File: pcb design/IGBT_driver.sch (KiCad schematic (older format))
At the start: 52 parts, among them J2 DESAT, Q13 NPN, Q14 PNP, U1 ISO5852S, U13 LM3480, U6 NAND, U8 TLP2745

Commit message: Changed power supply from 15/-8V to +15/-15V se we can make better use uf programmable -VEE. Changed connector to 14pos. Connected some missing signals. Updated layout
Signed-off-by: Marcos Chaparro <mchaparro@paltatech.com>
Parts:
- removed C53: 100nF, IPC7351-Nominal:CAPC1608X55, symbol C-0603
- removed D15: BAT54S, smd-semi:SOT-23, symbol BAT54S
- removed U6: NAND, smd-semi:SOT-23-5, symbol 741G00-SOT23
- added D15: 1N4148W, smd-semi:SOD-123, symbol 1N4148W
- added D17: GSOT03C, smd-semi:SOT-23, symbol BAT54A
- added R93: 330R, IPC7351-Nominal:RESC1608X50, symbol R-0603
- U8: value TLP2745 -> SI8710B; #mfg TLP2745(TP,E -> (none); mfg# (none) -> SI8710BD-B-IS; replacement SI8710BD-B-IS -> TLP2745(TP,E
- U8: value TLP2745 -> SI8710B; #mfg TLP2745(TP,E -> (none); mfg# (none) -> SI8710BD-B-IS
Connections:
- net labels added: -15V, IN-, PWM_VEE
- net labels removed: -8V
- wire segments 134 -> 135
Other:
- note added: "When FAULT is asserted\nexternally, mute the input"
- note added: "input protection.\nYou don't want a latch-up here"
- note removed: "Global Shutdown and reset configuration.\nEnsures that when ANY driver faults, all of\nthem are turned off. Datasheet: 10.2.2.5"
- note removed: "Input protection"
- note removed: "Inverts the signal so we\ncan use a positive logic\nAND fault mute-ing"
- moved on the sheet: C48, R42, R43, R45, TP13, TP14

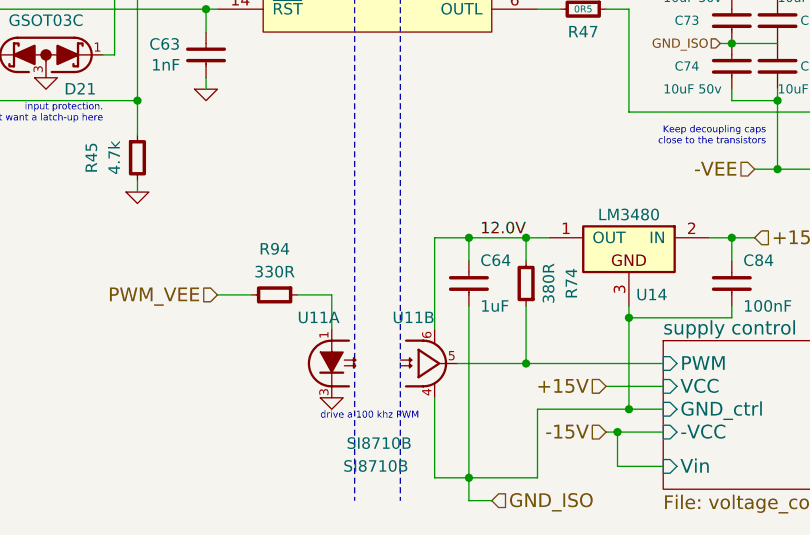
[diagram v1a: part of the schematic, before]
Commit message: Changed isolated amplifier from AMC1200 to AMC1301 because it has reinforced isolation. This required a different layout
Signed-off-by: Marcos Chaparro <mchaparro@paltatech.com>
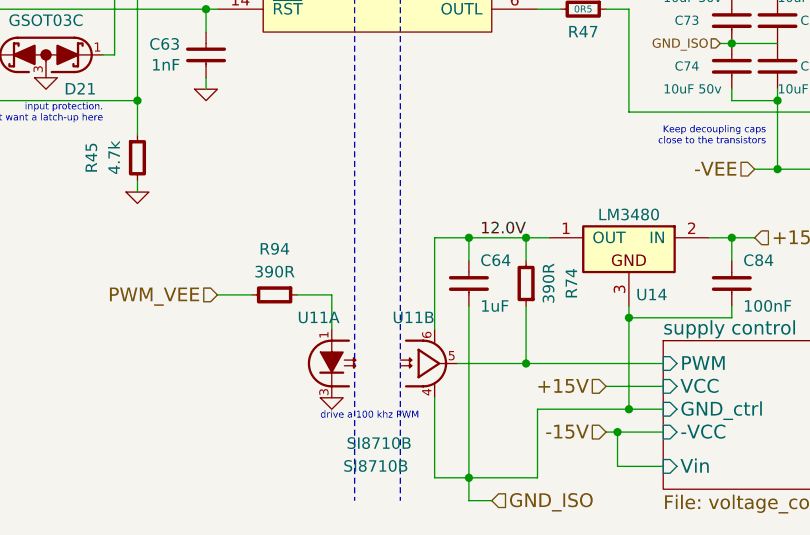
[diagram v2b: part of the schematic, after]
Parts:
- C16: mfg# (none) -> C0805C101J5GACTU
- D3, D4: #mfg MURS160-13-F -> (none); mfg# (none) -> MURS160-13-F
- R68: value 380R -> 390R; BOM RES SMD 1k 5% [0603] -> RES SMD 390R 1% [0603]; mfg# (none) -> RC0603FR-07390RL
- R93: value 330R -> 390R; BOM RES SMD 1k 5% [0603] -> RES SMD 390R 1% [0603]; mfg# (none) -> RC0603FR-07390RL
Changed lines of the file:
@@
 F 2 "Diodes_SMD:Diode-SMB_Standard" H 9500 4400 60  0001 C CNN
 F 3 "" H 9500 4400 60  0000 C CNN
-F 4 "MURS160-13-F" H 9500 4400 60  0001 C CNN "#mfg"
+F 4 "MURS160-13-F" H 9500 4400 60  0001 C CNN "mfg#"
 	1    9500 4400
 	0    -1   -1   0
@@
 F 2 "Diodes_SMD:Diode-SMB_Standard" H 10100 4400 60  0001 C CNN
 F 3 "" H 10100 4400 60  0000 C CNN
-F 4 "MURS160-13-F" H 10100 4400 60  0001 C CNN "#mfg"
+F 4 "MURS160-13-F" H 10100 4400 60  0001 C CNN "mfg#"
 	1    10100 4400
 	0    -1   -1   0
@@
 F 2 "IPC7351-Nominal:CAPC2012X70" H 8800 4600 50  0001 C CNN
 F 3 "" H 8790 4575 60  0000 C CNN
-F 4 "CAP MLCC 100pF C0G 50V 5% [0805]" H 9600 5150 60  0001 C CNN "BOM"
+F 4 "C0805C101J5GACTU" H 8800 4600 60  0001 C CNN "mfg#"
+F 5 "CAP MLCC 100pF C0G 50V 5% [0805]" H 9600 5150 60  0001 C CNN "BOM"
 	1    8800 4600
 	1    0    0    -1
@@
 AR Path="/58232371/58559E07" Ref="R?"  Part="1"
 F 0 "R74" V 4700 6100 50  0000 C CNN
-F 1 "380R" V 4800 6100 50  0000 C CNN
+F 1 "390R" V 4800 6100 50  0000 C CNN
 F 2 "IPC7351-Nominal:RESC1608X50" H 4900 6100 50  0001 C CNN
 F 3 "" H 4900 6150 60  0000 C CNN
-F 4 "RES SMD 1k 5% [0603]" H 5650 6650 60  0001 C CNN "BOM"
+F 4 "RC0603FR-07390RL" H 4900 6100 60  0001 C CNN "mfg#"
+F 5 "RES SMD 390R 1% [0603]" H 5650 6650 60  0001 C CNN "BOM"
 	1    4900 6100
 	-1   0    0    1
@@
 AR Path="/5824556D/58643F0A" Ref="R94"  Part="1"
 F 0 "R94" V 3600 6150 50  0000 C CNN
-F 1 "330R" V 3700 6150 50  0000 C CNN
+F 1 "390R" V 3700 6150 50  0000 C CNN
 F 2 "IPC7351-Nominal:RESC1608X50" H 3800 6150 50  0001 C CNN
 F 3 "" H 3800 6200 60  0000 C CNN
-F 4 "RES SMD 1k 5% [0603]" H 4550 6700 60  0001 C CNN "BOM"
+F 4 "RC0603FR-07390RL" H 3800 6150 60  0001 C CNN "mfg#"
+F 5 "RES SMD 390R 1% [0603]" H 4550 6700 60  0001 C CNN "BOM"
 	1    3800 6150
 	0    1    1    0

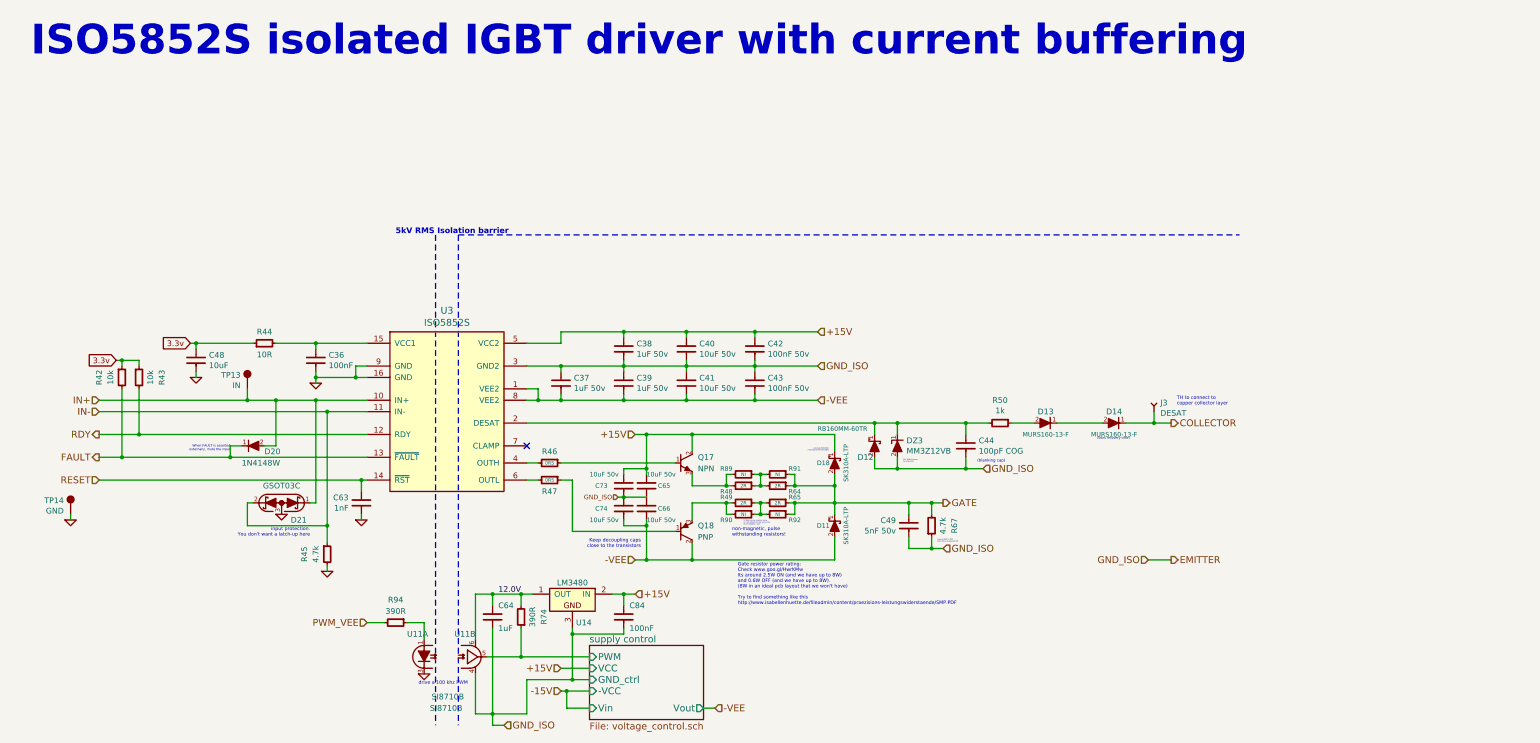
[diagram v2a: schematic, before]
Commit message: For some reasong eyrie needs the schematics and cache file synced
Signed-off-by: Marcos Chaparro <mchaparro@paltatech.com>
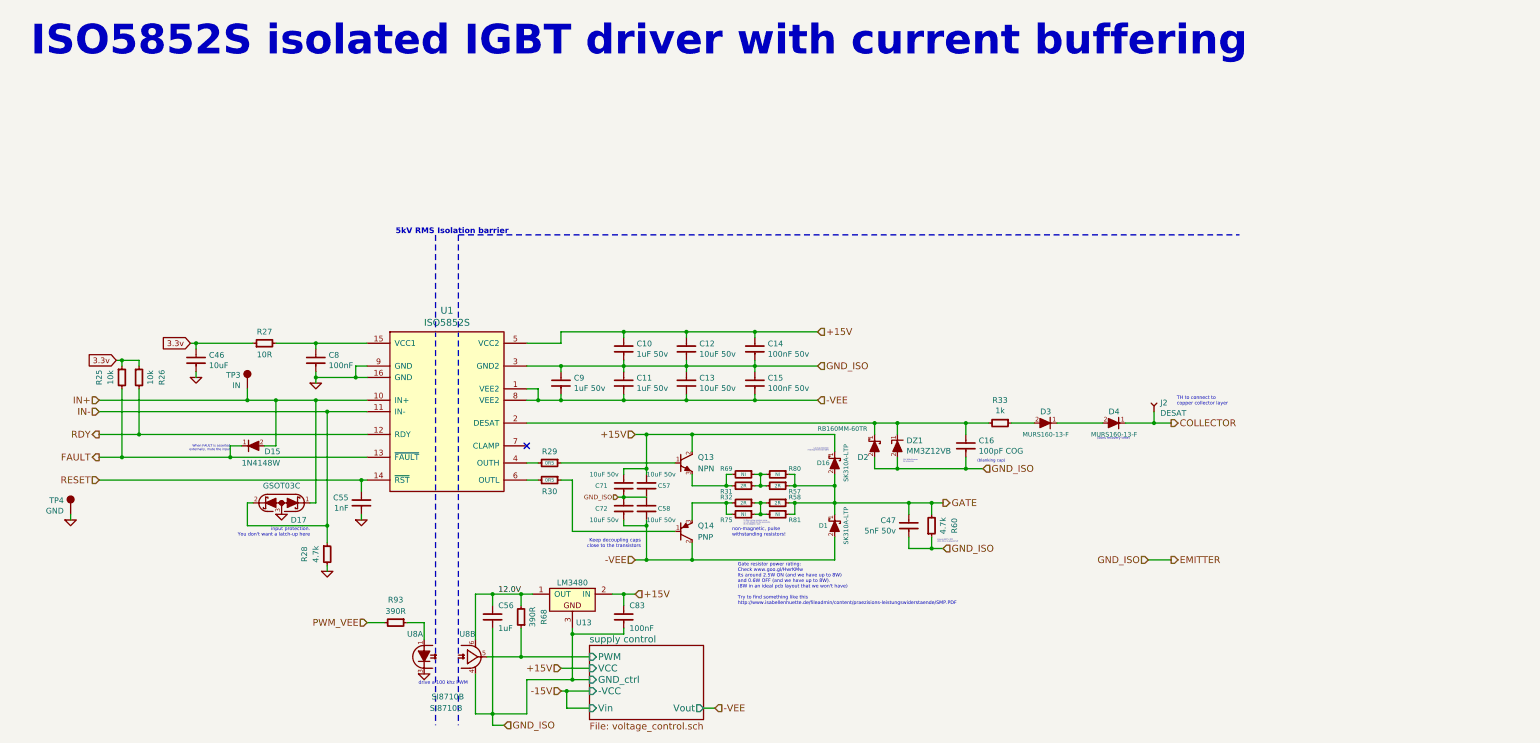
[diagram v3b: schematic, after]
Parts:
- U13: BOM IC MICROCHIP MCP1700T-vv02E/TT -> (none)

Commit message: Larger 2512 gate resistors
Signed-off-by: Marcos Chaparro <mchaparro@paltatech.com>
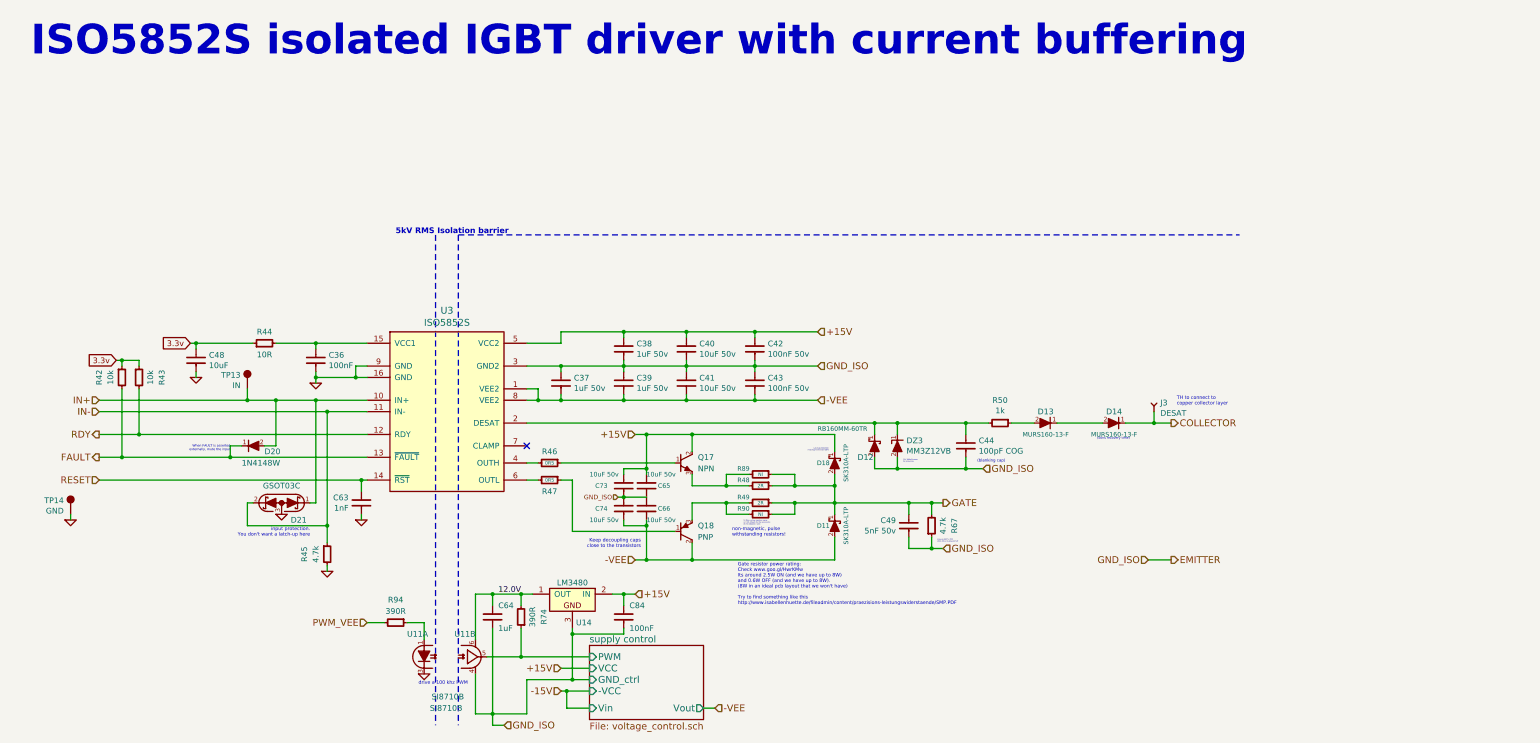
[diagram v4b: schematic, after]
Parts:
- removed R57, R58: 2R, IPC7351-Nominal:RESC3216X60, symbol R-0805
- removed R80, R81: NI, IPC7351-Nominal:RESC3216X60, symbol R-0805
- R31: footprint IPC7351-Nominal:RESC3216X60 -> IPC7351-Nominal:RESC6432X70
- R32, R75: footprint IPC7351-Nominal:RESC3216X60 -> IPC7351-Nominal:RESC6432X70; BOM RES SMD 2R 1% 2W +-100ppm [1206] -> RES SMD 2R 1% 2W +-100ppm [2512]
- R69: footprint IPC7351-Nominal:RESC3216X60 -> IPC7351-Nominal:RESC6432X70; #mfg PCNM1206K2R00FST5 -> (none); BOM RES SMD 2R 1% 2W +-100ppm [1206] -> (none)
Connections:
- net GATE: now also R31.1, R32.1, R69.1, R75.1
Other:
- moved on the sheet: R48, R49, R89, R90

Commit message: Added CERN Open Hardware Licence ("CERN OHL") version 1.2 documents
Signed-off-by: Marcos Chaparro <mchaparro@paltatech.com>
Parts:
- R31: value 2R -> 3R; #mfg PCNM1206K2R00FST5 -> (none); BOM RES SMD 2R 1% 2W +-100ppm [1206] -> RES SMD 3R 1% 2W +-100ppm [2512]; mfg# (none) -> PCNM2512K3R00FST5
- R32: value 2R -> 3R; #mfg PCNM1206K2R00FST5 -> (none); BOM RES SMD 2R 1% 2W +-100ppm [2512] -> RES SMD 3R 1% 2W +-100ppm [2512]; mfg# (none) -> PCNM2512K3R00FST5

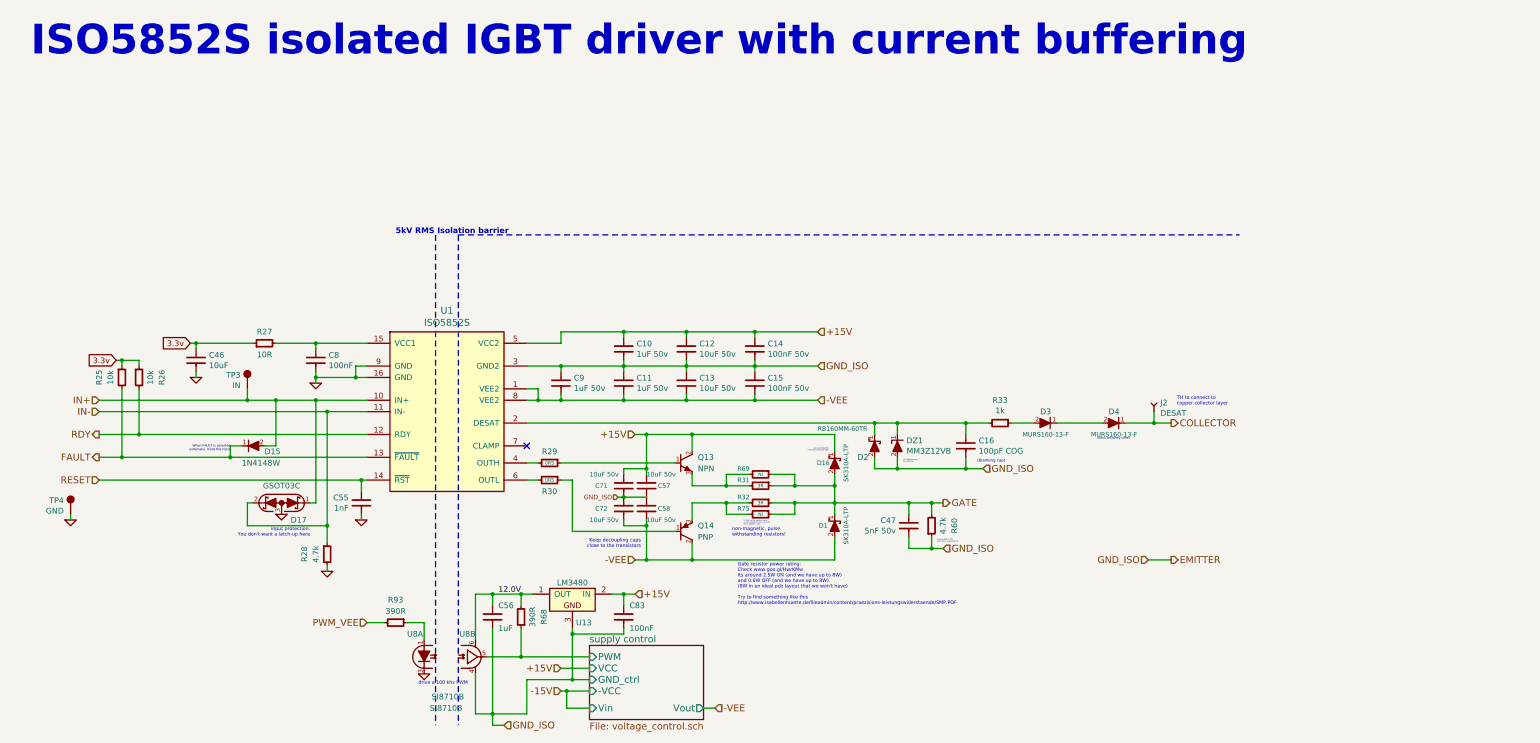
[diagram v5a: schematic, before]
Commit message: Added current sensor connector. Layout is now symmetrical
Signed-off-by: Marcos Chaparro <mchaparro@paltatech.com>
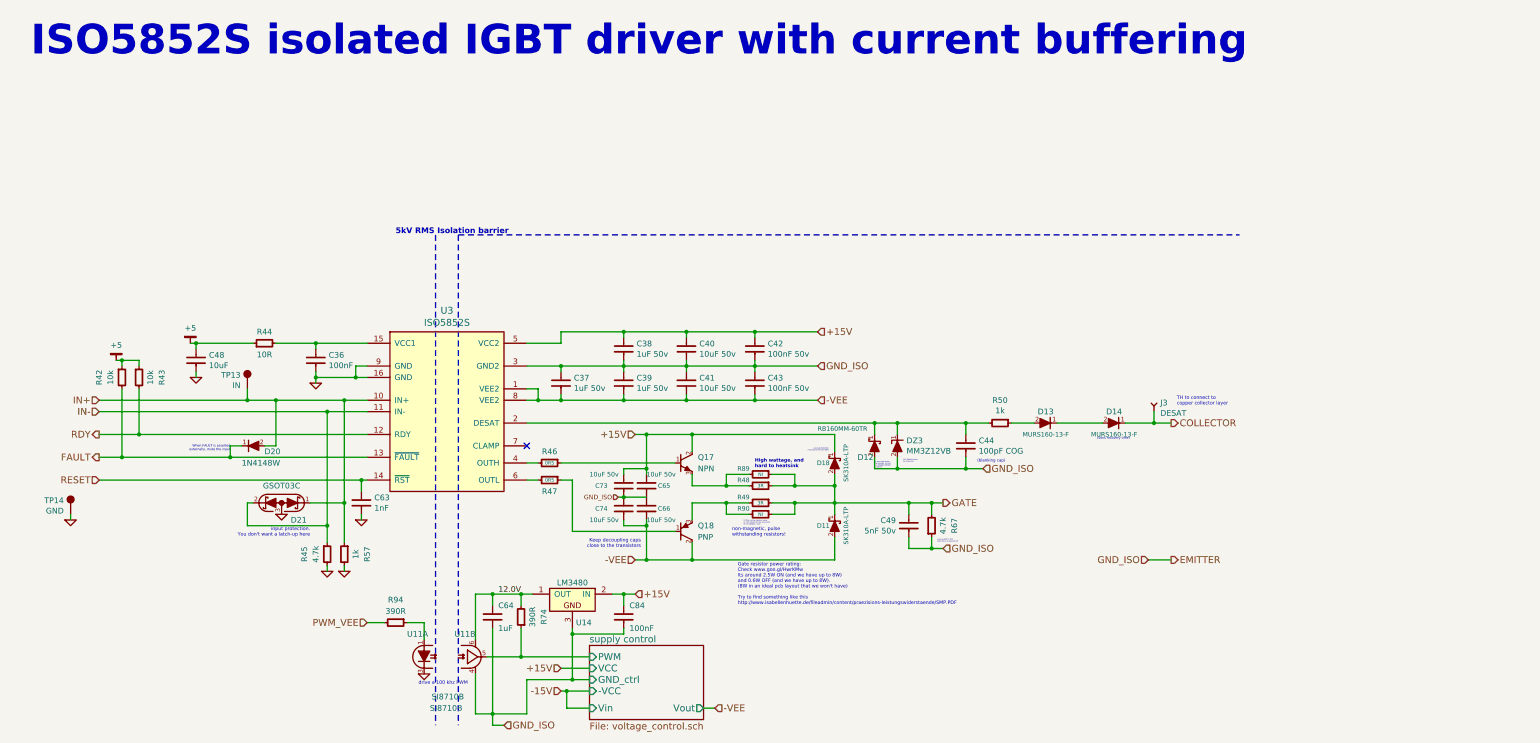
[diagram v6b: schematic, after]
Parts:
- added R58: 1k, IPC7351-Nominal:RESC1608X50, symbol R-0603
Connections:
- net GND: now also R58.2
- net IN+: now also R58.1
- net 3.3v renamed +5
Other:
- note added: "At very high temps\nthe leakage current\ncan DISABLE DESAT!\n(>100°C)"
- note added: "High wattage, and\nhard to heatsink"

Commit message: Add gate driver load to enable 2 step turnoff in buffered configuration. Updated layout.
Signed-off-by: Marcos Chaparro <mchaparro@paltatech.com>
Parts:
- added C87: 10nF, IPC7351-Nominal:CAPC1608X55, symbol pasv-cap:C-0603
- added D25: ES2J-LTP, IPC7351-Nominal:DIOM5226X203, symbol _semi:DIODE
- added DZ5: SMCJ440CA, IPC7351-Nominal:DIOM7959X265, symbol _semi:ZENER
- added R62: 12R, IPC7351-Nominal:RESC1608X50, symbol pasv-res:R-0603
- C10, C11, C9: symbol C-0805 -> pasv-cap:C-0805; MPN (none) -> CL21B105KBFNNNE
- C12, C13, C57, C58, C71, C72: symbol C-1206 -> pasv-cap:C-1206; MPN (none) -> CL31A106KBHNNNE; mfg# CL31B106KBHNNNE -> CL31A106KBHNNNE
- C14, C15: symbol C-0805 -> pasv-cap:C-0805; MPN (none) -> 08055C104JAT2A
- C16: symbol C-0805 -> pasv-cap:C-0805; MPN (none) -> C0805C101J5GACTU
- C46, C55, C56, C8, C83: symbol C-0603 -> pasv-cap:C-0603
- C47: symbol C-0805 -> pasv-cap:C-0805; mfg# CL21B105KBFNNNE -> (none)
- D1, D16: symbol SCHOTTKY -> _semi:SCHOTTKY; MPN (none) -> SK310A-LTP
- D15: symbol 1N4148W -> semi-diode-generic:1N4148W
- D17: symbol BAT54A -> semi-diode-generic:BAT54A; MPN (none) -> GSOT03C-E3-08
- D2: value RB160MM-60TR -> RB168MM-60TR; symbol SCHOTTKY -> _semi:SCHOTTKY; Exclude from BOM (none) -> 0; MPN (none) -> RB168MM-60TR; mfg# RB160MM-60TR -> RB168MM-60TR
- D3, D4: symbol DIODE -> _semi:DIODE; MPN (none) -> MURS160-13-F
- DZ1: symbol ZENER -> _semi:ZENER; MPN (none) -> MM3Z12VB
- J2: symbol CONN-100MIL-F-1x1 -> conn-100mil:CONN-100MIL-F-1x1
- Q13: symbol NPN -> _semi:NPN; MPN (none) -> MJD3055T4G
- Q14: symbol PNP -> _semi:PNP; MPN (none) -> MJD2955T4G
- R25, R26, R27, R28, R58: symbol R-0603 -> pasv-res:R-0603
- R29, R30: value 0R5 -> 12R; symbol R-0805 -> pasv-res:R-0805
- R31, R32: symbol R-0805 -> pasv-res:R-0805; MPN (none) -> PCNM2512K3R00FST5
- R33, R60, R69: symbol R-0805 -> pasv-res:R-0805
- R68, R93: symbol R-0603 -> pasv-res:R-0603; MPN (none) -> RC0603FR-07390RL
- R75: symbol R-0805 -> pasv-res:R-0805; MPN (none) -> PCNM1206K2R00FST5
- TP3, TP4: symbol TESTPOINT -> pcb:TESTPOINT; version (none) -> none
- U1: symbol ISO5852S -> paltatech:ISO5852S; MPN (none) -> ISO5852SQDWRQ1
- U13: symbol LM3480 -> IGBT_board-rescue:LM3480-RESCUE-IGBT_board; MPN (none) -> LM3480IM3X-12/NOPB
- U8: symbol TLP2745 -> IGBT_board-rescue:TLP2745-RESCUE-IGBT_board; MPN (none) -> SI8710BD-B-IS
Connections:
- net -VEE: now also C87.2
- net COLLECTOR: now also DZ5.1 (K)
- net GATE: now also D25.1 (K)
- net at R30.2, U1.6 (OUTL): now also R62.2
- net at Q13.1 (B), R29.1: now also Q14.1 (B), R30.1
- new net: C87.1, R62.1
- new net: D25.2 (A), DZ5.2 (A)
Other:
- note added: "(blanking cap)\nWith this cap you tune the desat response time.\nSiC mosfets need to enter soft turn off in less\nthan 3us.\nIGBTs have larger parasitic capacitance so its\nnot possible to use such short times. IGBTs\ncan withstand almost 10us."
- note added: "20uA leakage\nat 125°C"
- note added: "AEC Q-101: MJD44H11 and MJD45H11"
- note added: "Active overvoltage\nclamping for high\nfault current turn-off"
- note added: "ISO5852S isolated gate driver with current buffering"
- note added: "Needed for soft turn-off\nwhen current boost is \nused (tiduc70a 2.1.7)"
- note removed: "(blanking cap)"
- note removed: "At very high temps\nthe leakage current\ncan DISABLE DESAT!\n(>100°C)"
- note removed: "ISO5852S isolated IGBT driver with current buffering"
- moved on the sheet: C47, R60
